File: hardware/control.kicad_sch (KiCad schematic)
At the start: 15 parts, among them J7 ESP32_DISP_P1, J8 ESP32_DISP_CN1, J9 ESP32_DISP_P3, U1 MCP23017-E/SO, U2 TMP117MAIYBGR

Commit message: Rev0: named analog nets, both relay poles, HV netclass, smaller board
Restore the HV netclass (the real bug)
--------------------------------------
nanovolt-divider.kicad_dru conditions all three 450 V rules on NetClass == 'HV',
but the project file had "netclass_patterns": [] and no HV class, so every one of
them matched nothing. DRC reported "0 violations" whether the board was safe or
not. The original patterns matched auto-generated names like Net-(J3-Pin_1) and
were dropped when KiCad rewrote the project file.

The class is back with the patterns spelled out - /HV_IN_P and /HV_DIV, never a
"HV*" wildcard, which would sweep in HV_SENSE (a 3.3 V logic line). Verified by
moving R34 next to K5 on a scratch copy and confirming the rules fire; restoring
them immediately exposed 25 real clearance/creepage violations in the old
placement, now fixed.

gen_schematics.py no longer overwrites .kicad_pro (write_once): it emits a
25-line stub, and KiCad owns the 702-line file that holds the netclass.

Schematic
---------
* Analog nets carry real labels instead of /POLARITY (K4)/A_COM and
  Net-(J4-Pin_1): SRC_P, SRC_RTN, NORMAL_IN_P/N, RANGE_BUS, R*_IN, R*_OUT,
  INJ_NODE, MEAS_NODE, ANALOG_RTN, HV_IN_P, HV_DIV. This is also what gives the
  HV netclass stable patterns to match.
* K1..K3 use both poles: SRC_P -> A_COM -> A_NO -> R -> B_NO -> B_COM ->
  RANGE_BUS, so a deselected high leg is isolated at both ends.
* Control ground is DGND, not the global GND, so it cannot merge with the
  floating analog return.
* J7/J8/J9 use project symbols with the module's own pin names (SCL_IO22, IO35)
  instead of Conn_01x04 Pin_1..Pin_4. Pin geometry is unchanged, so no wire moved.
* Removed from the board: J4 (HV IN- is a panel-to-panel wire to SW1 lug 6), R26
  and SW1 lug 7 (R25's 100k already holds HV_SENSE low off the HV throw). Added
  C5 10 nF to stiffen the 100k against pickup on the IO35 harness. The two
  off-board lugs are documented in a panel-wiring note on the root sheet.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
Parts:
- removed R26: 10k, Resistor_SMD:R_1206_3216Metric, symbol Device:R
- added C5: 10n, Capacitor_SMD:C_1206_3216Metric, symbol Device:C
- J7: symbol Connector_Generic:Conn_01x04 -> nanovolt-divider:J_ESP32_P1
- J8: symbol Connector_Generic:Conn_01x04 -> nanovolt-divider:J_ESP32_CN1
- J9: symbol Connector_Generic:Conn_01x04 -> nanovolt-divider:J_ESP32_P3
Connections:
- net HV_SENSE: now also C5.1
- net GND renamed DGND
- net DGND: now also C5.2
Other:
- moved on the sheet: J7, J8, J9

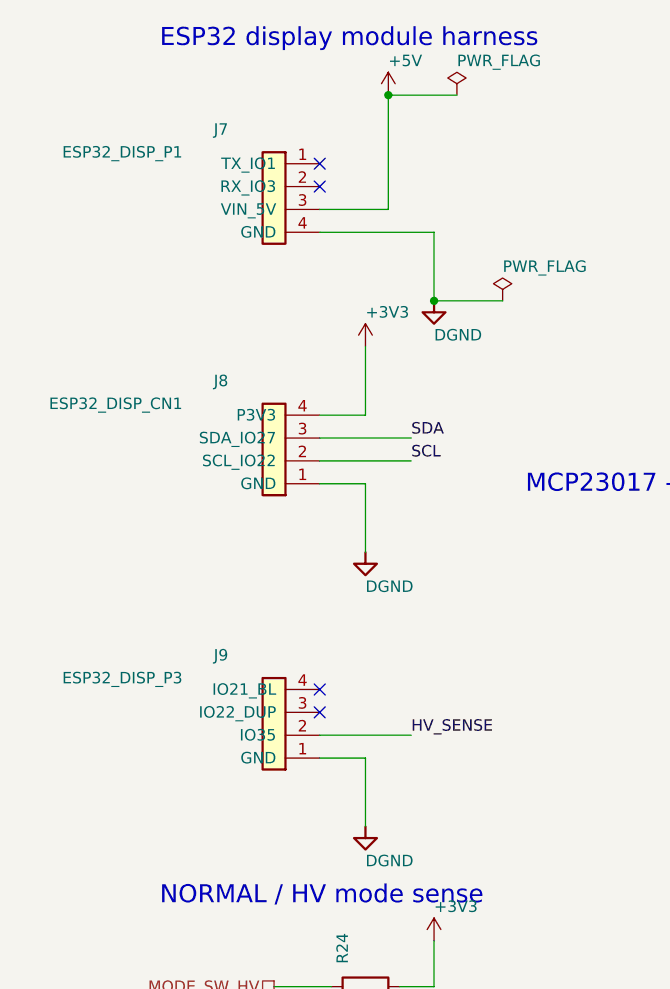
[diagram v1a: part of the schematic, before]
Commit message: Solder the display harness: J7-J9 become wire pads, board shrinks to 60x94
The board specified JST_XH_B4B-XH-A (2.50 mm) for J7/J8/J9, but the
ESP32-2432S028R's P1/CN1/P3 are 1.25 mm-class connectors.  That header
never mated with anything: it meant crimping a bespoke pitch-bridging
cable for a joint that never needs to unmate.  Solder the module's own
supplied pigtail to the board instead and the header, the crimping and
the pitch mismatch all go away at once.  The module end keeps its
connector, so the display still unplugs.

This also makes the board consistent - J1/J2/J3/J5/J6 are already
SolderWire pads and SW1 is a wire-pad footprint.  J7-J9 were the only
mateable connectors left on it.

Only the 8 live conductors get pads (J7 = P1 pins 3/4, J8 = CN1 pins
1-4, J9 = P3 pins 1/2), and each pad keeps the module's own pin number
rather than being renumbered 1..n, so the schematic still reads "this
wire lands on module P1 pin 3".  All three GND wires stay: P1's returns
the pulsed coil current, P3's is the HV_SENSE reference, CN1's serves
I2C - one net, but three conductors cut the cable-side IR drop.

Flat pads delete the top row's 5.75 mm bodies and their mating envelope,
freeing 6 mm: 60x100 -> 60x94, applied as one SHIFT_Y translation so
every reviewed relative spacing (slot geometry, HV island separation,
the 1 ohm strip, bridge widths) is unchanged.

Two things the regeneration turned up:
  * C5 landed 0.3 mm inside the top-right M3 hole's courtyard after the
    shift.  Moved to the second sub-row beside R25, its own pulldown.
  * The harness refdes silk ran off the board edge.  With the row 2.5 mm
    from the top there is one usable silk line below the pads, so it
    carries the module connector name (P1/CN1/P3) - what someone landing
    bare conductors actually needs - and the refdes moved to F.Fab.

Verified: ERC 0 violations.  DRC identical to the pre-change baseline
(67 pre-existing silk-over-copper on the unrouted board, 150 unconnected).
Netlist dif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
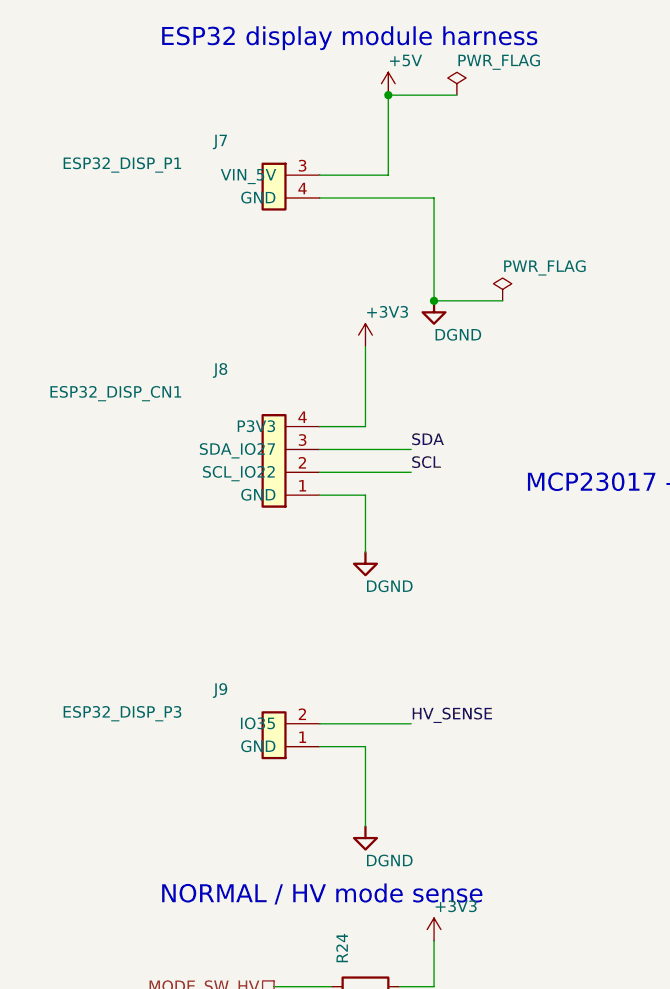
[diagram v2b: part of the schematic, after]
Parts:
- J7: footprint Connector_JST:JST_XH_B4B-XH-A_1x04_P2.50mm_Vertical -> nanovolt-divider:J_ESP32_P1_WirePads
- J8: footprint Connector_JST:JST_XH_B4B-XH-A_1x04_P2.50mm_Vertical -> nanovolt-divider:J_ESP32_CN1_WirePads
- J9: footprint Connector_JST:JST_XH_B4B-XH-A_1x04_P2.50mm_Vertical -> nanovolt-divider:J_ESP32_P3_WirePads
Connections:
- no-connect marks 15 -> 11

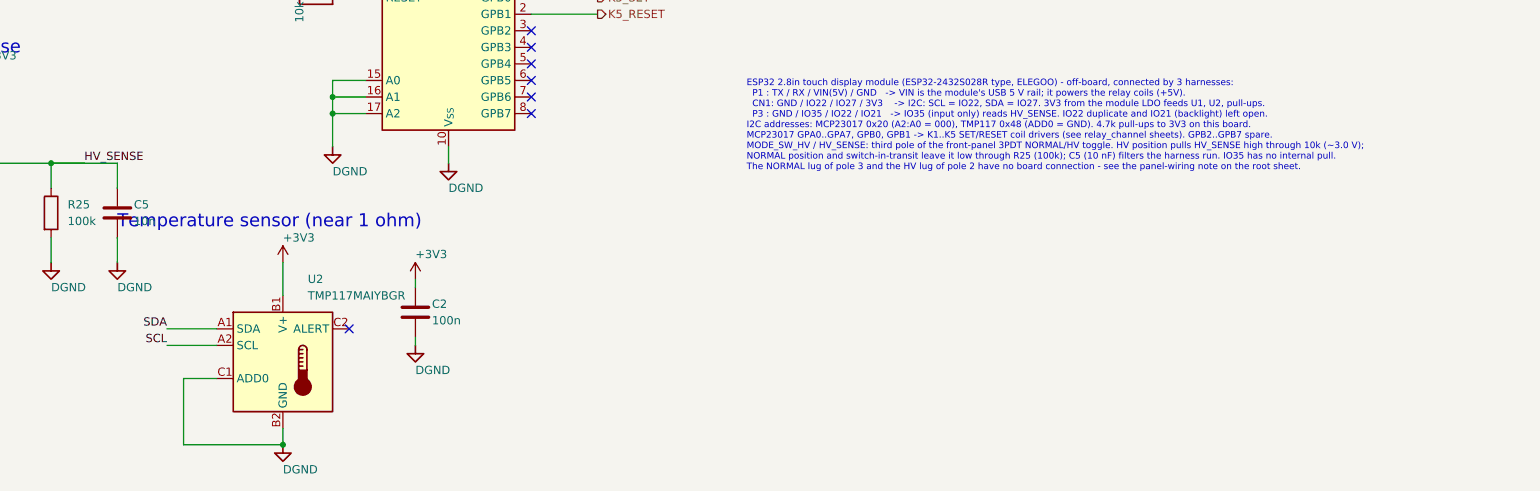
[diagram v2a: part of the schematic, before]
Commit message: Swap the TMP117 for a TMP275: SOIC-8, so it can be hand-soldered
The TMP117 only ships as a DSBGA-6 on a 0.4 mm ball pitch, which is not
hand-assemblable, and this board is built by hand. TMP275AIDR is SOIC-8
at 1.27 mm pitch and keeps address 0x48 (A2:A0 all on DGND), so nothing
else on the I2C bus moves.

The cost is absolute accuracy: +/-0.5 C and 12-bit (0.0625 C) instead of
+/-0.1 C and 16-bit (0.0078 C). That is not what this sensor is for - it
tracks the *change* in the 1 ohm region's temperature for the optional
ratio correction, and that needs short-term repeatability, not absolute
accuracy. The register map is not TMP117-compatible, so firmware will
differ when it is written.

Schematic: new project symbol nanovolt-divider:TMP275. KiCad 10 has no
TMP275 - the pinout is the LM75/TMP75 industry-standard one, so
Sensor_Temperature:LM75B would have wired up correctly, but it would put
"LM75B" in the lib_id and call pin 3 "O.S." instead of ALERT. The body is
17.78 mm wide so the rotated V+ / GND pin names clear "ALERT".

Board: a SOIC-8 courtyard is 5.4 mm tall and the band between the
isolation slots and R35 was 5.38 mm, so the sensor no longer fits in the
gap over the resistor body. It sits on the same thermally isolated island
above R35, centred on the resistor's midpoint, 0.7 mm below the slots and
0.8 mm above R35's courtyard - the island is what couples it to R35, not
the millimetre of air over the body. The 1 ohm row dropped 1.5 mm to make
the room, taken from the bottom margin so the slots, the mounting holes
and everything above them stay where the Rev0 review left them.

U2's designator moves to F.Fab and R35's to its pad-1 end (new
REF_OVERRIDE table in gen_pcb.py): there is no silk line left between a
SOIC-8 and a 20 mm resistor sharing a 6.9 mm band. The DSBGA 0.1 mm
intra-footprint DRC exception is gone from the .kicad_dru with the part
that needed it.

ERC 0 violations. The netlist diff is confined to U2's pins. DRC 66
violations against a 67 bas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
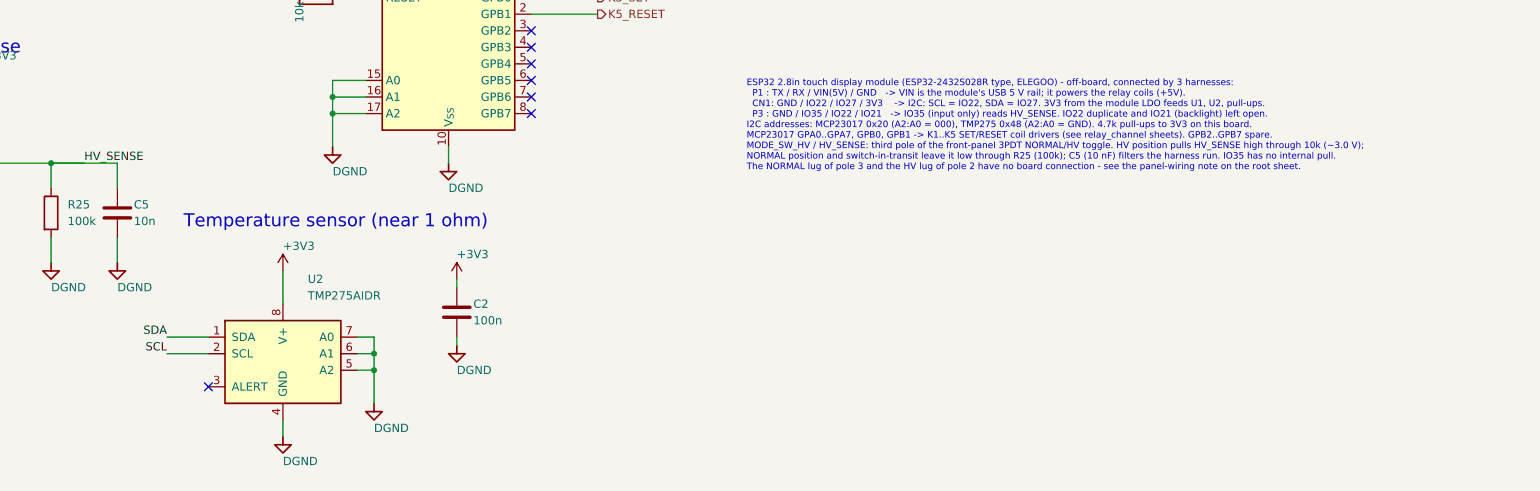
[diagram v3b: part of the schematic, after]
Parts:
- U2: value TMP117MAIYBGR -> TMP275AIDR; footprint Package_BGA:Texas_DSBGA-6_0.95x1.488mm_Layout2x3_P0.4mm -> Package_SO:SOIC-8_3.9x4.9mm_P1.27mm; symbol Sensor_Temperature:TMP117xxYBG -> nanovolt-divider:TMP275; MPN TMP117MAIYBGR -> TMP275AIDR
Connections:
- net +3V3: now also U2.8 (V+); no longer U2.B1 (V+)
- net DGND: now also U2.4 (GND), U2.5 (A2), U2.6 (A1), U2.7 (A0); no longer U2.B2 (GND), U2.C1 (ADD0)
- net SCL: now also U2.2 (SCL); no longer U2.A2 (SCL)
- net SDA: now also U2.1 (SDA); no longer U2.A1 (SDA)
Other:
- title: Control: ESP32 display module interface, MCP23017 relay drivers, TMP117 -> Control: ESP32 display module interface, MCP23017 relay drivers, TMP275

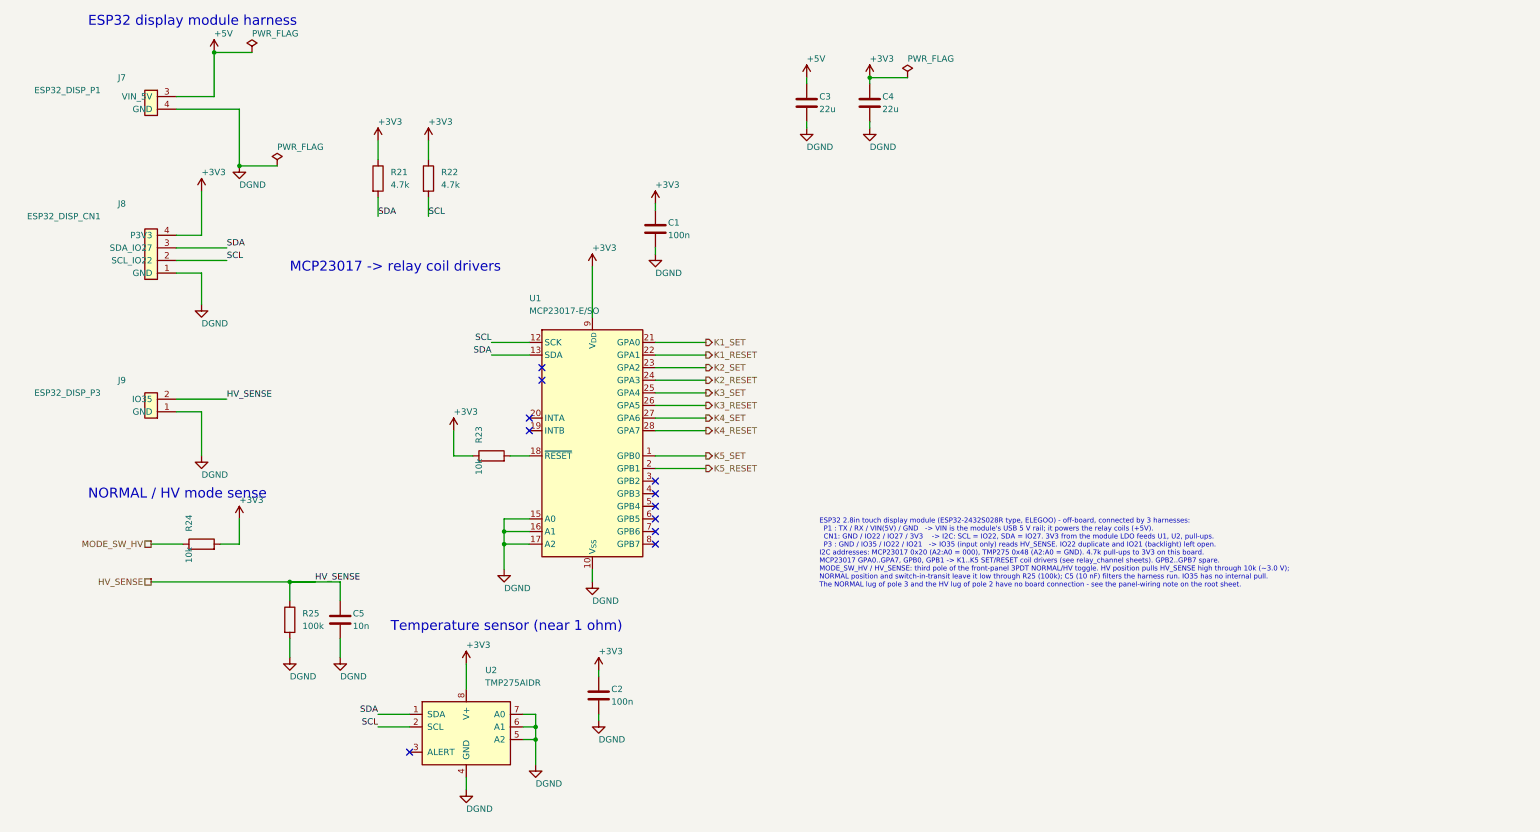
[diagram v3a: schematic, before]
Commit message: Remove the 450 V path: keep the instrument single-purpose
The HV input shared the 1 ohm low leg, and that shared leg capped what the
range could ever be. At 10 M the divider drew 45 uA and gave 45 uV out;
more output meant a smaller high leg, and 1 M draws 450 uA where 10 M
draws 45 uA. A Geiger supply is built to source microamps into a tube that
draws almost none, so its output impedance is high - often set by a series
anode resistor. Against a 1 M source impedance a 10 M divider already
reads 9% low and a 1 M divider reads 50% low, and that error tracks the
supply's operating point, so calibration cannot remove it.

The HV path also had no polarity reversal - K4 serves the NORMAL input
only - so thermal EMF and DMM offset could not be nulled by ABBA the way
they are on the normal ranges. More output was exactly what that path
needed, and the shared 1 ohm leg was the one thing that would not give it.

A dedicated fixed divider has none of those constraints because it picks
its own low leg, so the 450 V measurement moves out of this instrument.

SW1's two analog poles were only ever selecting between the normal path
and the HV path, so with the HV path gone both collapse to plain nets:
K5 A_NO lands directly on MEAS_NODE and B_NO directly on ANALOG_RTN.
ISOLATE is untouched - K5 was always what performed it.

Removed: R34, J3, SW1 and the panel toggle, R24/R25/C5, the J9/P3
harness, the SW_3PDT symbol and its wire-pad footprint, the J_ESP32_P3
symbol and footprint, the HV netclass (generator template and the live
.kicad_pro), and all three HV rules from .kicad_dru - which is now down to
the single bridge-track-width rule. 71 components to 64. The panel is four
banana jacks with nothing wired panel-to-panel, so every conductor now
appears in the netlist.

Board 60 x 94 -> 60 x 83. Getting the full 11 mm needed one extra move:
J1/J2 sat below the relay row, directly above the lower-left mounting
hole, which pinned that hole and through it the slots and the whole 1 oh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
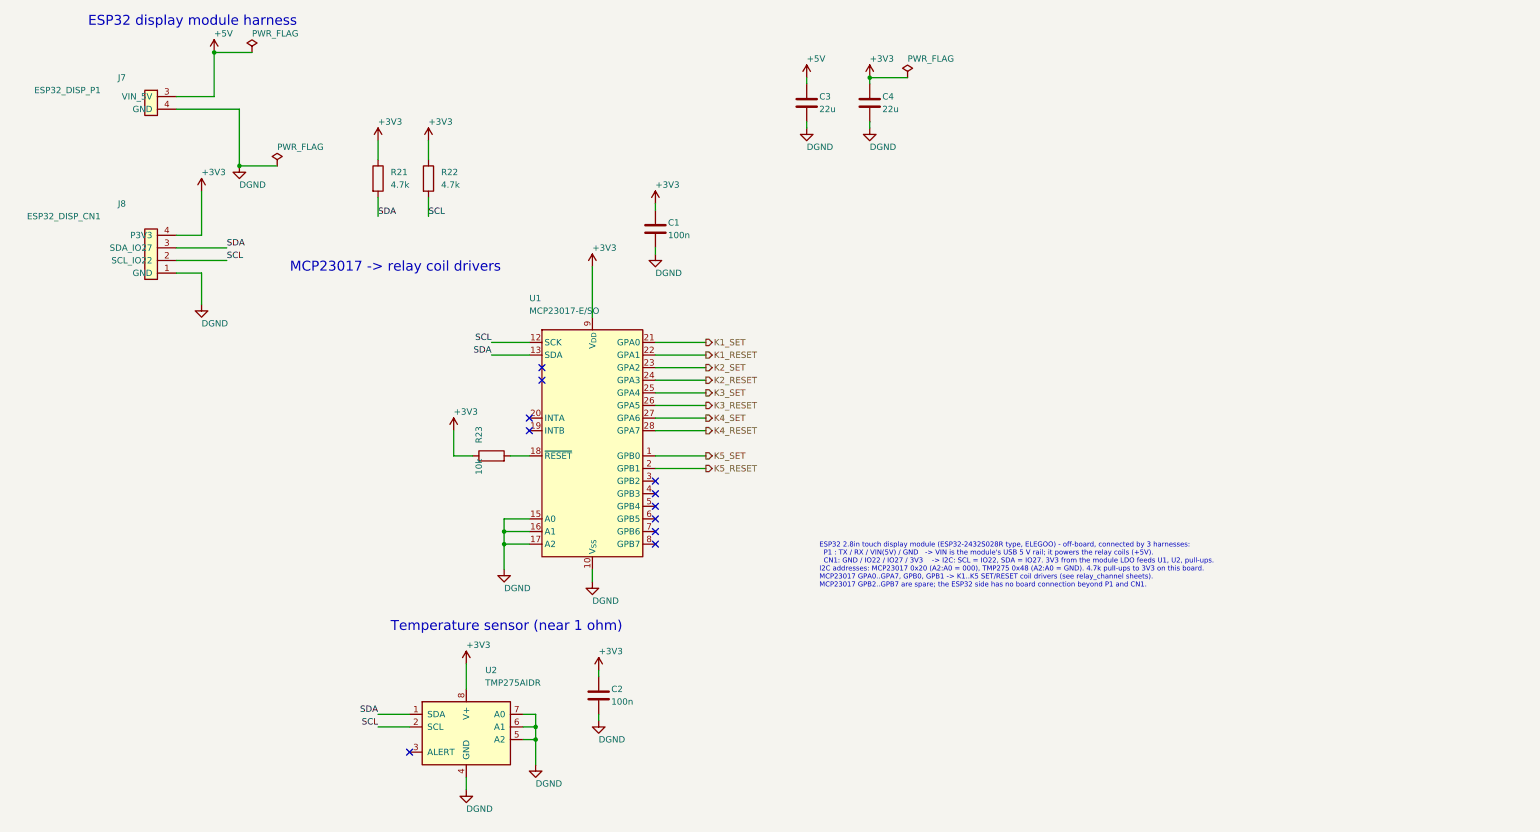
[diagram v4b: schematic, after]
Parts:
- removed C5: 10n, Capacitor_SMD:C_1206_3216Metric, symbol Device:C
- removed J9: ESP32_DISP_P3, nanovolt-divider:J_ESP32_P3_WirePads, symbol nanovolt-divider:J_ESP32_P3
- removed R24: 10k, Resistor_SMD:R_1206_3216Metric, symbol Device:R
- removed R25: 100k, Resistor_SMD:R_1206_3216Metric, symbol Device:R
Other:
- note added: "ESP32 2.8in touch display module (ESP32-2432S028R type, ELEGOO) - off-board, connected by 3 harnesses: P1 : TX / RX / VIN(5V) / GND -> VIN is the module's USB 5 V rail; it powers the relay coils (+5V). CN1: GND / IO22 / IO27 / 3V3 -> I2C: SCL = IO22, SDA = IO27. 3V3 from the module LDO feeds U1, U2, pull-ups. I2C addresses: MCP23017 0x20 (A2:A0 = 000), TMP275 0x48 (A2:A0 = GND). 4.7k pull-ups to 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"
- note removed: "ESP32 2.8in touch display module (ESP32-2432S028R type, ELEGOO) - off-board, connected by 3 harnesses: P1 : TX / RX / VIN(5V) / GND -> VIN is the module's USB 5 V rail; it powers the relay coils (+5V). CN1: GND / IO22 / IO27 / 3V3 -> I2C: SCL = IO22, SDA = IO27. 3V3 from the module LDO feeds U1, U2, pull-ups. P3 : GND / IO35 / IO22 / IO21 -> IO35 (input only) reads HV_SENSE. IO22 duplicate and IO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"
- note removed: "NORMAL / HV mode sense"
